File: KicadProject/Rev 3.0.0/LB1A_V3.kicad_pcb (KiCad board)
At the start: 6 copper layers, 45 x 45 mm, 193 parts, among them J601 2337019-1, J602 2337019-1, U101 STM32MP157CAA3, U201 AS4C256M16D3LC-12BCN, U401 STPMIC1xPQR, U501 S40FC004C1B2C00000, U601 LBEE59B1LV-278, U701 DF40C-100DP-0.4V(51), U702 DF40C-100DP-0.4V(51), U703 DF40C-100DP-0.4V(51), X101 32.768kHz, Y101 24MHz

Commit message: working on pmic layout
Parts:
- U101: value STM32MP157CAA3 -> LFBGA448_18X18
- moved C402 134.7 mm to (106.4, 98.7), turned to 180 degrees
- moved C418 131.6 mm to (112.8, 95.4), turned to 180 degrees
- moved C419 129.6 mm to (105.8, 96.1), turned to 270 degrees
- moved L401 126.0 mm to (112.6, 97.5)
- moved L402 124.5 mm to (107.9, 96.2), turned to 90 degrees
- moved C401 122.9 mm to (110.1, 98.0), turned to 90 degrees
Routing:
- added copper zone on L2_Gnd.Cu, net GND

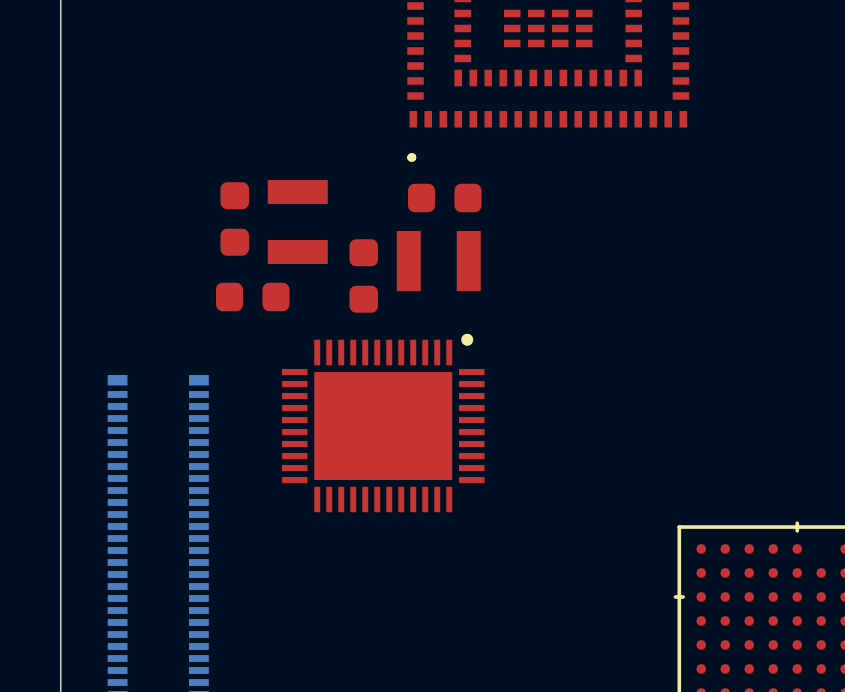
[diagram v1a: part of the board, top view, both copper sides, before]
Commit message: Updated location of PMIC
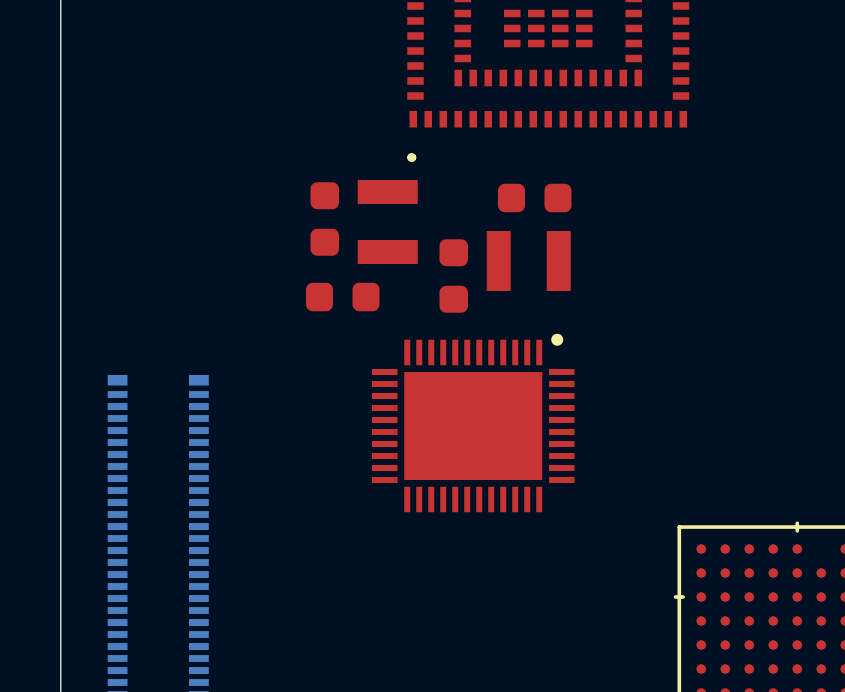
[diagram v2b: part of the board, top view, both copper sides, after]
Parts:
- moved C401 3.00 mm to (113.1, 98.0)
- moved C402 3.00 mm to (109.4, 98.7)
- moved C418 3.00 mm to (115.8, 95.4)
- moved C419 3.00 mm to (108.8, 96.1)
- moved L401 3.00 mm to (115.6, 97.5)
- moved L402 3.00 mm to (110.9, 96.2)
- moved U401 3.00 mm to (113.8, 103.0)
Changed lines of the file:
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@@
   )
   (module U_Package_QFN:STPMIC1BPQR (layer L1_Sig_Pwr.Cu)
-    (at 110.75 103 270)
+    (at 113.75 103 270)
     (descr STPMIC1)
     (tags "Integrated Circuit")
@@
   )
   (module U_Inductor_SMD:MGV2520101R0M-10 (layer L1_Sig_Pwr.Cu)
-    (at 107.9 96.2 90)
+    (at 110.9 96.2 90)
     (fp_text reference L402 (at 0.382 -1.9064 90) (layer F.SilkS) hide
       (effects (font (size 0.6 0.6) (thickness 0.09)))
@@
   )
   (module U_Inductor_SMD:MGV2520101R0M-10 (layer L1_Sig_Pwr.Cu)
-    (at 112.6 97.5)
+    (at 115.6 97.5)
     (fp_text reference L401 (at 0.382 -1.9064) (layer F.SilkS) hide
       (effects (font (size 0.6 0.6) (thickness 0.09)))
@@
   )
   (module U_Capacitor_SMD:C_0603_1608Metric (layer L1_Sig_Pwr.Cu)
-    (at 105.8 96.1 270)
+    (at 108.8 96.1 270)
     (descr "Capacitor SMD 0603 (1608 Metric), square (rectangular) end terminal, IPC_7351 nominal, (Body size source: IPC-SM-782 page 76, https://www.pcb-3d.com/wordpress/wp-content/uploads/ipc-sm-782a_amendment_1_and_2.pdf), generated with kicad-footprint-generator")
     (tags capacitor)
@@
   )
   (module U_Capacitor_SMD:C_0603_1608Metric (layer L1_Sig_Pwr.Cu)
-    (at 112.8 95.4 180)
+    (at 115.8 95.4 180)
     (descr "Capacitor SMD 0603 (1608 Metric), square (rectangular) end terminal, IPC_7351 nominal, (Body size source: IPC-SM-782 page 76, https://www.pcb-3d.com/wordpress/wp-content/uploads/ipc-sm-782a_amendment_1_and_2.pdf), generated with kicad-footprint-generator")
     (tags capacitor)
@@
   )
   (module U_Capacitor_SMD:C_0603_1608Metric (layer L1_Sig_Pwr.Cu)
-    (at 106.4 98.7 180)
+    (at 109.4 98.7 180)
     (descr "Capacitor SMD 0603 (1608 Metric), square (rectangular) end terminal, IPC_7351 nominal, (Body size source: IPC-SM-782 page 76, https://www.pcb-3d.com/wordpress/wp-content/uploads/ipc-sm-782a_amendment_1_and_2.pdf), generated with kicad-footprint-generator")
     (tags capacitor)
@@
   )
   (module U_Capacitor_SMD:C_0603_1608Metric (layer L1_Sig_Pwr.Cu)
-    (at 110.1 98 90)
+    (at 113.1 98 90)
     (descr "Capacitor SMD 0603 (1608 Metric), square (rectangular) end terminal, IPC_7351 nominal, (Body size source: IPC-SM-782 page 76, https://www.pcb-3d.com/wordpress/wp-content/uploads/ipc-sm-782a_amendment_1_and_2.pdf), generated with kicad-footprint-generator")
     (tags capacitor)

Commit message: pmic placement 1
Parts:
- C408, C409, C420, R401, R402: moved to B.Cu
- moved C404 141.4 mm to (108.6, 107.4), turned to 180 degrees
- moved R401 138.2 mm to (115.5, 106.9), turned to 270 degrees
- moved R402 133.1 mm to (118.4, 104.3)
- moved L404 127.9 mm to (111.4, 108.3), turned to 270 degrees
- moved C408 122.9 mm to (118.6, 106.4), turned to 270 degrees
- moved C403 122.7 mm to (113.5, 108.1), turned to 270 degrees
- moved C420 121.8 mm to (113.5, 108.5), turned to 90 degrees
- moved C421 119.0 mm to (108.6, 109.2), turned to 180 degrees
- moved C409 115.7 mm to (117.0, 106.4), turned to 90 degrees
- moved L403 113.8 mm to (115.6, 108.3), turned to 270 degrees
- moved U201 0.45 mm to (129.8, 95.2)

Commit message: pmic placement 2
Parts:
- C405, C415, C416: moved to B.Cu
- moved C406 156.3 mm to (91.0, 113.4)
- moved C413 153.0 mm to (90.9, 115.1)
- moved C414 139.0 mm to (108.5, 105.4)
- moved C412 136.4 mm to (108.5, 100.6)
- moved C411 136.1 mm to (108.5, 102.2)
- moved C415 128.9 mm to (112.9, 102.6), turned to 180 degrees
- moved C405 127.9 mm to (110.0, 100.2), turned to 180 degrees
- moved C416 124.8 mm to (112.9, 104.2), turned to 180 degrees
- moved C407 121.4 mm to (108.5, 103.8), turned to 180 degrees
- moved C409 3.45 mm to (115.3, 103.4), turned to 270 degrees
- moved C420 0.89 mm to (114.3, 108.9), turned to 180 degrees
- moved R401 0.78 mm to (116.1, 106.4), turned to 0 degrees
- moved C408 0.40 mm to (118.2, 106.4)

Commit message: pmic placement 3
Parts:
- C101, C406, C410, C413: moved to B.Cu
- moved C410 124.9 mm to (119.3, 103.0)
- moved C417 124.3 mm to (119.0, 103.0), turned to 180 degrees
- moved R106 115.3 mm to (118.1, 101.2), turned to 270 degrees
- moved R104 109.9 mm to (120.1, 101.2), turned to 270 degrees
- moved R105 106.3 mm to (119.1, 101.2), turned to 270 degrees
- moved C101 105.0 mm to (118.1, 100.2), turned to 90 degrees
- moved C413 19.3 mm to (108.6, 107.4)
- moved C406 19.2 mm to (108.5, 105.4), turned to 180 degrees
- moved C405 1.55 mm to (108.5, 100.6)

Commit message: pmic complete
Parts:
- moved C418 0.32 mm to (115.7, 95.7)
- moved C419 0.30 mm to (108.8, 96.4)
- moved C402 0.30 mm to (109.4, 99.0)
- moved L401 0.30 mm to (115.6, 97.8)
- moved L402 0.30 mm to (110.9, 96.5)
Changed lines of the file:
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@@
   )
   (module U_Inductor_SMD:MGV2520101R0M-10 (layer L1_Sig_Pwr.Cu)
-    (at 110.9 96.2 90)
+    (at 110.9 96.5 90)
     (fp_text reference L402 (at 0.382 -1.9064 90) (layer F.SilkS) hide
       (effects (font (size 0.6 0.6) (thickness 0.09)))
@@
   )
   (module U_Inductor_SMD:MGV2520101R0M-10 (layer L1_Sig_Pwr.Cu)
-    (at 115.6 97.5)
+    (at 115.6 97.8)
     (fp_text reference L401 (at 0.382 -1.9064) (layer F.SilkS) hide
       (effects (font (size 0.6 0.6) (thickness 0.09)))
@@
   )
   (module U_Capacitor_SMD:C_0603_1608Metric (layer L1_Sig_Pwr.Cu)
-    (at 108.8 96.1 270)
+    (at 108.8 96.4 270)
     (descr "Capacitor SMD 0603 (1608 Metric), square (rectangular) end terminal, IPC_7351 nominal, (Body size source: IPC-SM-782 page 76, https://www.pcb-3d.com/wordpress/wp-content/uploads/ipc-sm-782a_amendment_1_and_2.pdf), generated with kicad-footprint-generator")
     (tags capacitor)
@@
   )
   (module U_Capacitor_SMD:C_0603_1608Metric (layer L1_Sig_Pwr.Cu)
-    (at 115.8 95.4 180)
+    (at 115.7 95.7 180)
     (descr "Capacitor SMD 0603 (1608 Metric), square (rectangular) end terminal, IPC_7351 nominal, (Body size source: IPC-SM-782 page 76, https://www.pcb-3d.com/wordpress/wp-content/uploads/ipc-sm-782a_amendment_1_and_2.pdf), generated with kicad-footprint-generator")
     (tags capacitor)
@@
   )
   (module U_Capacitor_SMD:C_0603_1608Metric (layer L1_Sig_Pwr.Cu)
-    (at 109.4 98.7 180)
-    (descr "Capacitor SMD 0603 (1608 Metric), square (rectangular) end terminal, IPC_7351 nominal, (Body size source: IPC-SM-782 page 76, https://www.pcb-3d.com/wordpress/wp-content/uploads/ipc-sm-782a_amendment_1_and_2.pdf), generated with kicad-footprint-generator")
-    (tags capacitor)
+    (at 109.4 99 180)
+    (descr "Capacitor SMD 0603 (1608 Metric), square (rectangular) end terminal, IPC_7351 nominal, (Body size source: IPC-SM-782 page 76, https://www.pcb-3d.com/wordpress/wp-content/uploads/ipc-sm-782a_amendment_1_and_2.pdf), generated with kicad-footprint-generator")
+    (tags capacitor)

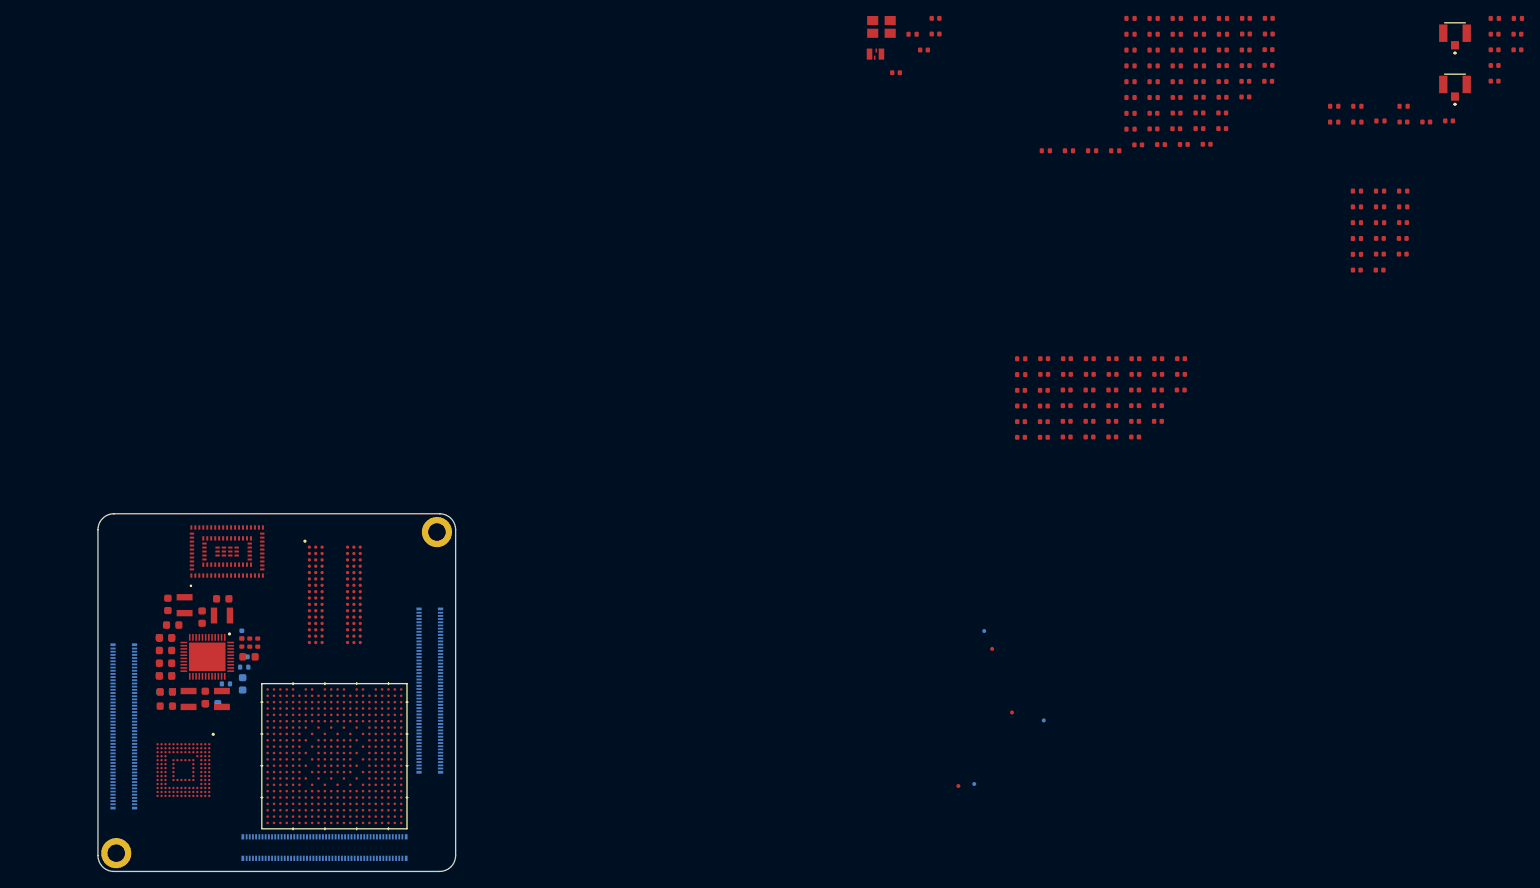
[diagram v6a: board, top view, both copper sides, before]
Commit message: eMMC also done
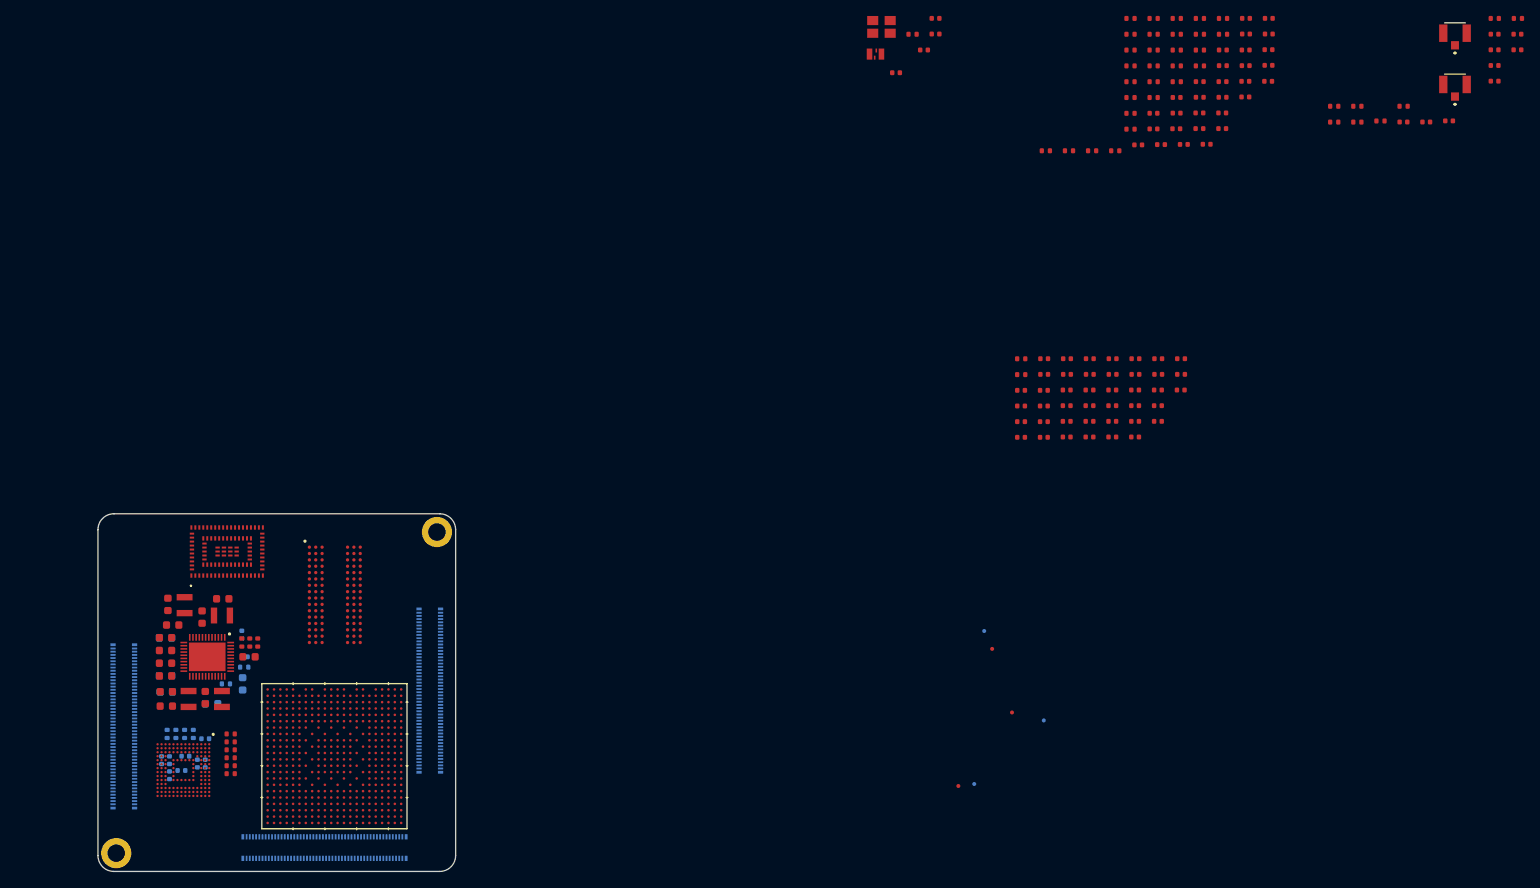
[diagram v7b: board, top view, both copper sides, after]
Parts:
- added C508: 2.2uF, U_Capacitor_SMD:C_0402_1005Metric, B.Cu at (113.5, 113.3)
- C501, C502, C503, C504, C505, C506, R506, R507, R509, R510: moved to B.Cu
- C507: value 2.2uF -> 4.7uF; moved to B.Cu
- U101: value LFBGA448_18X18 -> STM32MP157CAA3
- moved C502 170.2 mm to (108.0, 116.0), turned to 270 degrees
- moved C507 167.7 mm to (109.0, 116.0), turned to 270 degrees
- moved R510 167.2 mm to (108.7, 112.7), turned to 270 degrees
- moved R507 167.0 mm to (110.9, 112.7), turned to 270 degrees
- moved C505 165.4 mm to (112.5, 116.4), turned to 90 degrees
- moved C506 163.4 mm to (110.5, 117.3), turned to 180 degrees
- moved C504 163.0 mm to (111.0, 115.5), turned to 180 degrees
- moved R506 162.6 mm to (112.0, 112.7), turned to 90 degrees
- moved R504 162.6 mm to (116.7, 112.7), turned to 180 degrees
- moved C503 162.3 mm to (109.0, 117.9), turned to 90 degrees
- moved C501 161.9 mm to (113.5, 116.4), turned to 90 degrees
- moved R503 160.8 mm to (116.7, 116.7), turned to 180 degrees
- moved R509 160.4 mm to (109.8, 112.7), turned to 270 degrees
- moved R508 159.5 mm to (116.7, 117.7), turned to 180 degrees
- moved R502 157.7 mm to (116.7, 115.7), turned to 180 degrees
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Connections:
- C507 pad 1: Net-(C507-Pad1) -> PMIC_LDO5_2V9
- U501 pad C1: Net-(C507-Pad1) -> Net-(C508-Pad1)
- U501 pad C2: Net-(C507-Pad1) -> Net-(C508-Pad1)

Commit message: wireless module placement
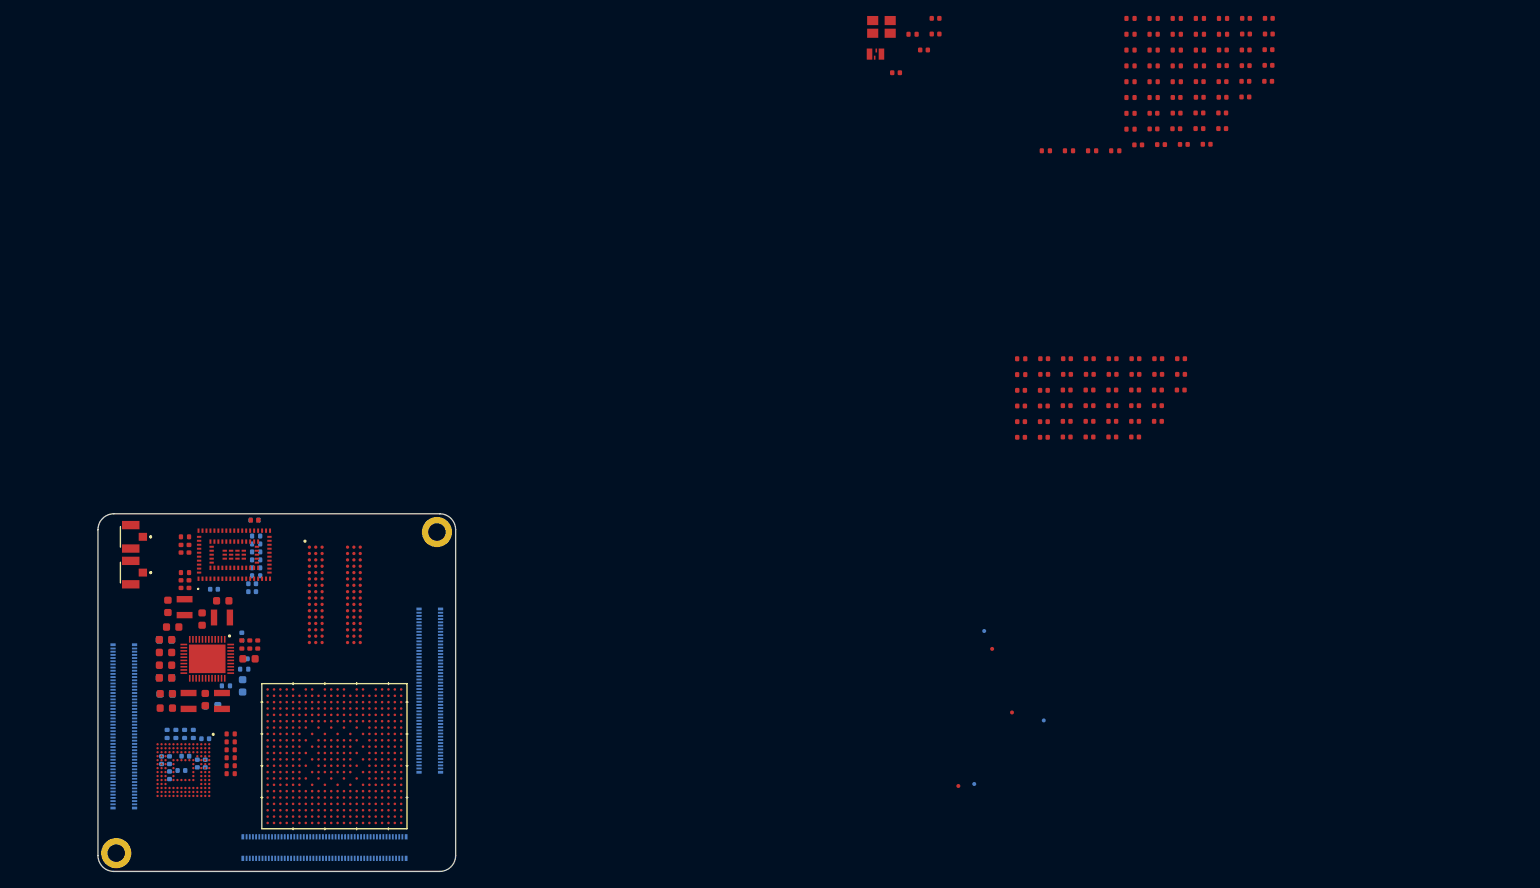
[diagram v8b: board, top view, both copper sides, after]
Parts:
- C601, C606, C607, C609, R603, R604, R605, R606, R607, R608: moved to B.Cu
- U101: value STM32MP157CAA3 -> LFBGA448_18X18
- moved C604 180.9 mm to (111.5, 93.8), turned to 270 degrees
- moved C602 178.5 mm to (111.5, 89.4), turned to 270 degrees
- moved J601 178.3 mm to (104.1, 87.9), turned to 90 degrees
- moved J602 177.6 mm to (104.1, 92.4), turned to 90 degrees
- moved R601 177.2 mm to (111.0, 87.9)
- moved C603 176.1 mm to (110.5, 89.4), turned to 270 degrees
- moved R608 171.6 mm to (119.9, 87.8)
- moved C607 170.9 mm to (119.4, 93.8)
- moved C605 167.1 mm to (110.5, 93.8), turned to 270 degrees
- moved C609 166.9 mm to (119.7, 85.8)
- moved C601 166.2 mm to (114.6, 94.5)
- moved C608 165.5 mm to (119.7, 85.8)
- moved R602 158.7 mm to (111.0, 92.4)
- moved C606 156.4 mm to (119.4, 94.8)
- moved R604 155.6 mm to (119.9, 91.8)
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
